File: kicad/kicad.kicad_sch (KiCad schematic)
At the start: 9 parts, among them Q1 BPW40, Q2 BP103BF, U1 PIC16F18875-E/P, U2 L293D

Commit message: finished schematic
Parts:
- added C1, C2: 0.1uF, symbol Device:C_Polarized_US
- added C3: 1000uF, symbol Device:C_Polarized_US
- added C4: C_Polarized_US, symbol Device:C_Polarized_US
- added D2: D, symbol Device:D
- added DS1: WC1602A, Display:WC1602A, symbol Display_Character:WC1602A
- added J1: ~, symbol Connector:Screw_Terminal_01x03
- added M1: Fan, symbol Motor:Fan
- added M2: Left, symbol Motor:Motor_DC
- added M3: Right, symbol Motor:Motor_DC
- added Q3: NPN, symbol Simulation_SPICE:NPN
- added R5, R6: R, symbol Device:R
- added RV1: 100k, symbol Device:R_Potentiometer
- added U3, U4: TSSP58038, OptoDevice:Vishay_MINICAST-3Pin, symbol Sensor_Proximity:TSSP58038
- added U5: L7805, symbol Regulator_Linear:L7805
- U1: footprint PDIP40_P_MCH -> (none)
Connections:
- net +5V: now also U2.16 (VCC1), U2.8 (VCC2), C1.1, C2.1, C3.1, C4.1, DS1.15 (LED(+)), DS1.2 (VDD), R5.1, R6.2, RV1.1, U3.3 (Vs), U4.3 (Vs), U5.3 (OUT)
- net GND: now also U2.12 (GND), U2.13 (GND), U2.4 (GND), U2.5 (GND), C1.2, C2.2, C3.2, C4.2, DS1.1 (VSS), DS1.16 (LED(-)), J1.2 (Pin_2), J1.3 (Pin_3), Q3.3 (E), RV1.3, U3.2 (GND), U4.2 (GND), U5.2 (GND)
- net at U2.1 (EN1,2): now also R5.2
- net RMF: now reaches U2.10 (3A)
- net RMF: now also U1.21 (RD2)
- net at U2.11 (3Y): now also M3.1 (+)
- net at U2.14 (4Y): now also M3.2 (-)
- net RMB: now reaches U2.15 (4A)
- net RMB: now also U1.22 (RD3)
- net LMF: now reaches U2.2 (1A)
- net LMF: now also U1.19 (RD0)
- net at U2.3 (1Y): now also M2.1 (+)
- net at U2.6 (2Y): now also M2.2 (-)
- net LMB: now reaches U2.7 (2A)
- net LMB: now also U1.20 (RD1)
- net at U2.9 (EN3,4): now also R6.1
- net at U1.33 (RB0): now also DS1.4 (RS)
- net at U1.34 (RB1): now also DS1.5 (R/W)
- net at U1.35 (RB2): now also DS1.6 (E)
- net at U1.37 (RB4): now also DS1.11 (D4)
- net at U1.38 (RB5): now also DS1.12 (D5)
- net at U1.39 (RB6/ICSPCLK): now also DS1.13 (D6)
- net at U1.40 (RB7/ICSPDAT): now also DS1.14 (D7)
- net at U1.5 (RA3): now also U3.1 (OUT)
- net at U1.6 (RA4): now also U4.1 (OUT)
- net fan: now reaches U1.7 (RA5)
- net fan: now also Q3.2 (B)
- new net: D2.2 (A), M1.2 (-), Q3.1 (C)
- new net: DS1.3 (VO), RV1.2
- new net +12V: D2.1 (K), M1.1 (+)
- new net +9V: J1.1 (Pin_1), U5.1 (IN)

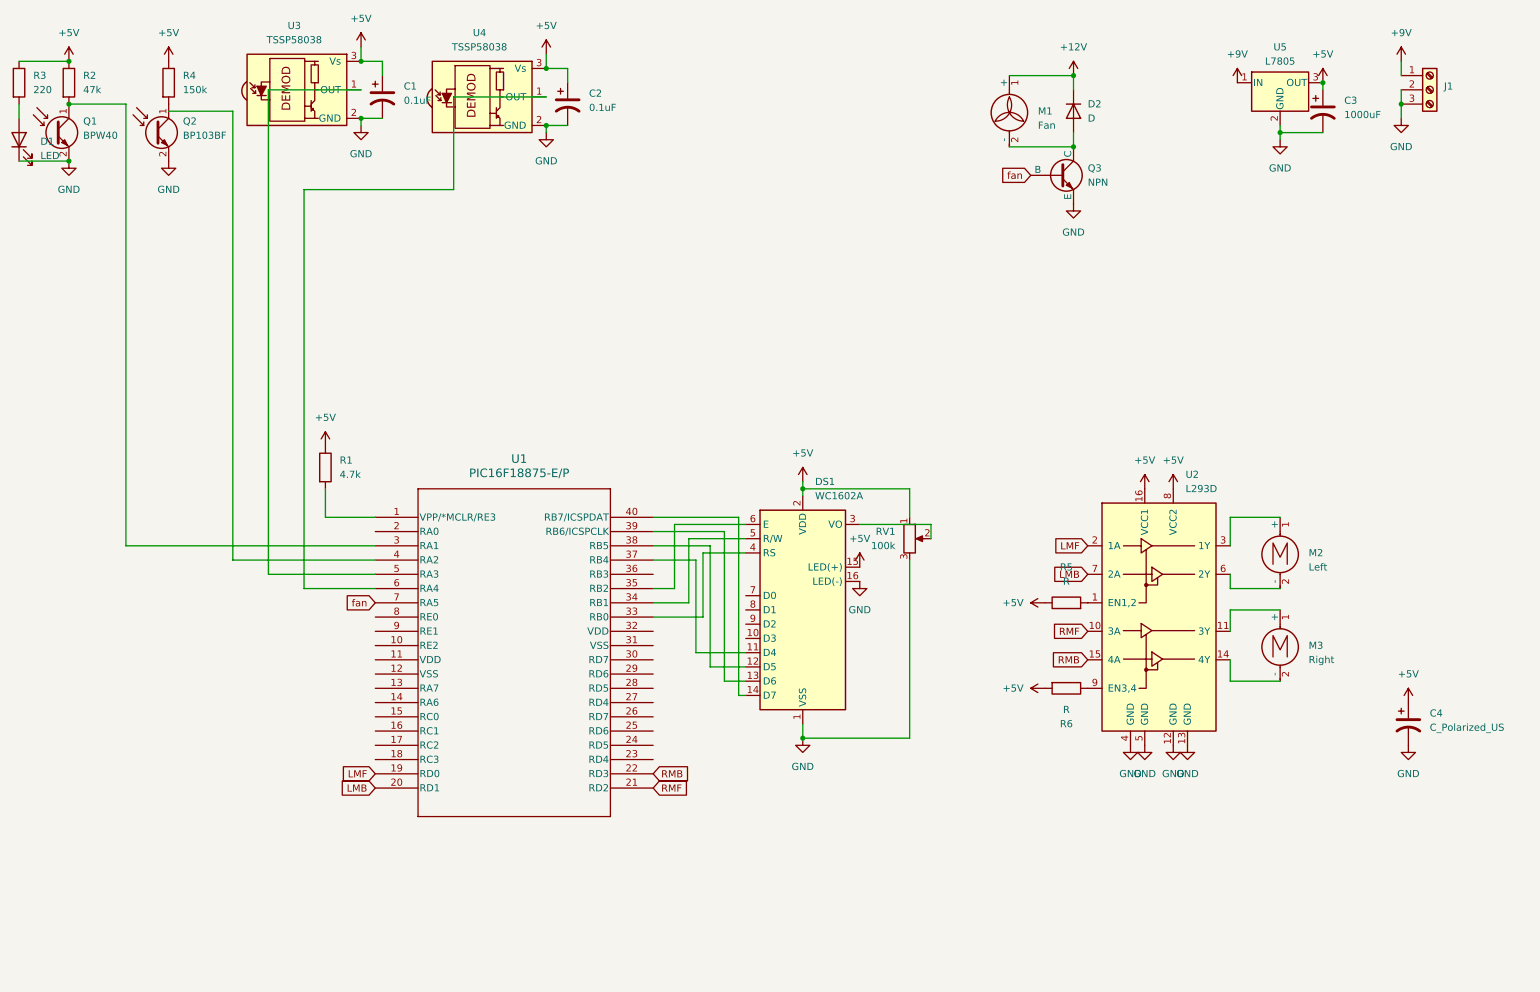
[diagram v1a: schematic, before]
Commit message: linked all footprints
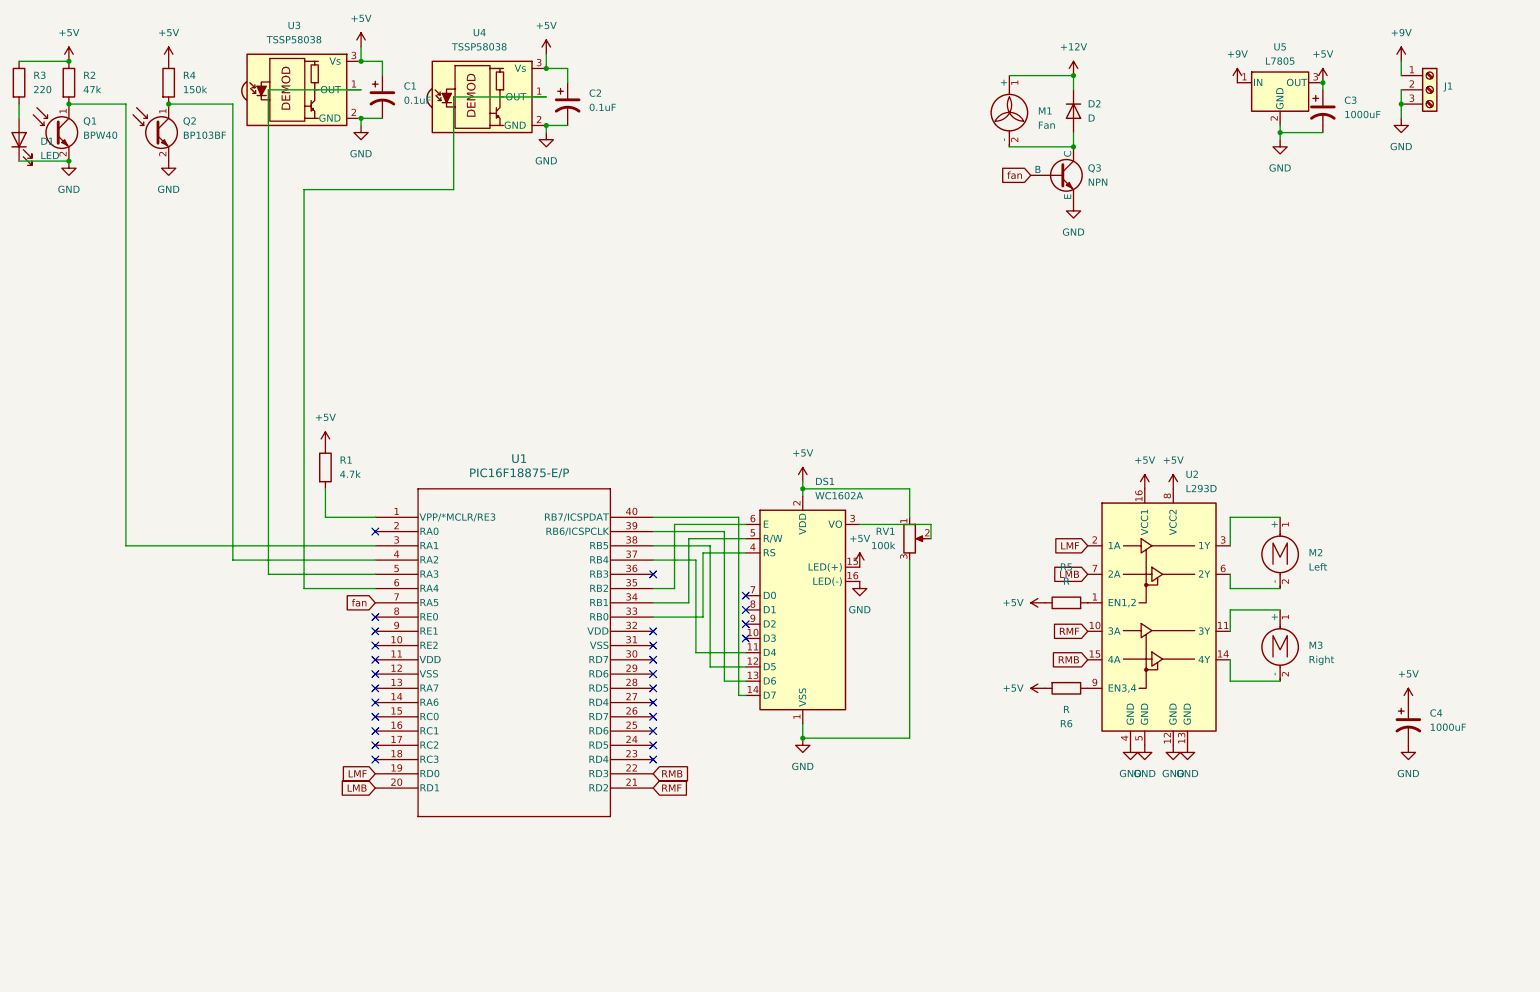
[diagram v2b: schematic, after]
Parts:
- C1, C2: footprint (none) -> EZ_TEJ_Library:C_Disc_D4.3mm_W1.9mm_P5.00mm
- C3: footprint (none) -> EZ_TEJ_Library:CP_Radial_D8.0mm_P3.80mm
- C4: value C_Polarized_US -> 1000uF; footprint (none) -> EZ_TEJ_Library:CP_Radial_D8.0mm_P3.80mm
- D1, M1, M2, M3: footprint (none) -> EZ_TEJ_Library:SolderWire-0.5sqmm_1x02_P4.6mm_D0.9mm_OD2.1mm
- D2: footprint (none) -> EZ_TEJ_Library:D_DO-41_SOD81_P7.62mm_Horizontal
- J1: footprint (none) -> EZ_TEJ_Library:TerminalBlock_Phoenix_PT-1,5-3-5.0-H_1x03_P5.00mm_Horizontal
- Q3: footprint (none) -> EZ_TEJ_Library:TO-92_Inline_Wide
- R1, R2, R3, R4, R5, R6: footprint (none) -> EZ_TEJ_Library:R_Axial_DIN0207_L6.3mm_D2.5mm_P7.62mm_Horizontal
- RV1: footprint (none) -> Potentiometer_THT:Potentiometer_Bourns_3386P_Vertical
- U1: footprint (none) -> EZ_TEJ_Library:DIP-40_W15.24mm_LongPads
- U5: footprint (none) -> EZ_TEJ_Library:TO-220-3_Vertical
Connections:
- net at Q2.1 (C), R4.2: now also U1.4 (RA2)
- no-connect marks 0 -> 27
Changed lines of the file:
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@@
 	)
 	(junction
+		(at 46.99 31.75)
+		(diameter 0)
+		(color 0 0 0 0)
+	)
+	(junction
 		(at 266.7 31.75)
 		(diameter 0)
 		(color 0 0 0 0)
 	)
+	(no_connect
+		(at 149.86 127)
+	)
+	(no_connect
+		(at 83.82 146.05)
+	)
+	(no_connect
+		(at 83.82 135.89)
+	)
+	(no_connect
+		(at 133.35 140.97)
+	)
+	(no_connect
+		(at 149.86 121.92)
+	)
+	(no_connect
+		(at 83.82 125.73)
+	)
+	(no_connect
+		(at 83.82 130.81)
+	)
+	(no_connect
+		(at 83.82 138.43)
+	)
+	(no_connect
+		(at 83.82 148.59)
+	)
+	(no_connect
+		(at 83.82 133.35)
+	)
+	(no_connect
+		(at 149.86 119.38)
+	)
+	(no_connect
+		(at 83.82 143.51)
+	)
+	(no_connect
+		(at 133.35 143.51)
+	)
+	(no_connect
+		(at 133.35 128.27)
+	)
+	(no_connect
+		(at 133.35 135.89)
+	)
+	(no_connect
+		(at 83.82 140.97)
+	)
+	(no_connect
+		(at 83.82 123.19)
+	)
+	(no_connect
+		(at 133.35 138.43)
+	)
+	(no_connect
+		(at 133.35 130.81)
+	)
+	(no_connect
+		(at 83.82 107.95)
+	)
+	(no_connect
+		(at 133.35 115.57)
+	)
+	(no_connect
+		(at 83.82 128.27)
+	)
+	(no_connect
+		(at 133.35 125.73)
+	)
+	(no_connect
+		(at 149.86 124.46)
+	)
+	(no_connect
+		(at 133.35 133.35)
+	)
+	(no_connect
+		(at 133.35 146.05)
+	)
+	(no_connect
+		(at 133.35 148.59)
+	)
 	(wire
 		(pts
@@
 	(wire
 		(pts
-			(xy 46.99 33.02) (xy 58.42 33.02)
+			(xy 46.99 31.75) (xy 58.42 31.75)
 		)
 		(stroke
@@
 	(wire
 		(pts
-			(xy 58.42 33.02) (xy 58.42 113.03)
+			(xy 58.42 31.75) (xy 58.42 113.03)
 		)
 		(stroke
@@
 			)
 		)
-		(property "Footprint" ""
+		(property "Footprint" "EZ_TEJ_Library:SolderWire-0.5sqmm_1x02_P4.6mm_D0.9mm_OD2.1mm"
 			(at 245.11 129.286 0)
 			(effects
@@
 			)
 		)
-		(property "Footprint" ""
+		(property "Footprint" "EZ_TEJ_Library:R_Axial_DIN0207_L6.3mm_D2.5mm_P7.62mm_Horizontal"
 			(at 73.152 96.52 90)
 			(effects
@@
 			)
 		)
-		(property "Value" "C_Polarized_US"
+		(property "Value" "1000uF"
 			(at 271.78 142.8749 0)
 			(effects
@@
 			)
 		)
-		(property "Footprint" ""
+		(property "Footprint" "EZ_TEJ_Library:CP_Radial_D8.0mm_P3.80mm"
 			(at 267.97 142.24 0)
 			(effects
@@
 			)
 		)
-		(property "Footprint" ""
+		(property "Footprint" "EZ_TEJ_Library:C_Disc_D4.3mm_W1.9mm_P5.00mm"
 			(at 85.09 30.48 0)
 			(effects
@@
 			)
 		)
-		(property "Footprint" ""
+		(property "Footprint" "EZ_TEJ_Library:TO-220-3_Vertical"
 			(at 245.745 31.75 0)
 			(effects
@@
 			)
 		)
-		(property "Footprint" ""
+		(property "Footprint" "EZ_TEJ_Library:R_Axial_DIN0207_L6.3mm_D2.5mm_P7.62mm_Horizontal"
 			(at 207.01 122.428 90)
 			(effects
@@
 			)
 		)
-		(property "Footprint" ""
+		(property "Footprint" "EZ_TEJ_Library:R_Axial_DIN0207_L6.3mm_D2.5mm_P7.62mm_Horizontal"
 			(at 45.212 27.94 90)
 			(effects
@@
 			)
 		)
-		(property "Footprint" ""
+		(property "Footprint" "EZ_TEJ_Library:D_DO-41_SOD81_P7.62mm_Horizontal"
 			(at 208.28 33.02 0)
 			(effects
@@
 			)
 		)
-		(property "Footprint" ""
+		(property "Footprint" "EZ_TEJ_Library:R_Axial_DIN0207_L6.3mm_D2.5mm_P7.62mm_Horizontal"
 			(at 18.542 27.94 90)
 			(effects
@@
 			)
 		)
-		(property "Footprint" ""
+		(property "Footprint" "EZ_TEJ_Library:C_Disc_D4.3mm_W1.9mm_P5.00mm"
 			(at 118.11 31.75 0)
 			(effects
@@
 			)
 		)
-		(property "Footprint" ""
+		(property "Footprint" "EZ_TEJ_Library:SolderWire-0.5sqmm_1x02_P4.6mm_D0.9mm_OD2.1mm"
 			(at 20.32 38.1 0)
 			(effects
@@
 			)
 		)
-		(property "Footprint" ""
+		(property "Footprint" "EZ_TEJ_Library:CP_Radial_D8.0mm_P3.80mm"
 			(at 252.73 33.02 0)
 			(effects
@@
 			)
 		)
-		(property "Footprint" ""
+		(property "Footprint" "EZ_TEJ_Library:SolderWire-0.5sqmm_1x02_P4.6mm_D0.9mm_OD2.1mm"
 			(at 196.85 34.036 0)
 			(effects
@@
 			)
 		)
-		(property "Footprint" ""
+		(property "Footprint" "EZ_TEJ_Library:TO-92_Inline_Wide"
 			(at 269.24 44.45 0)
 			(effects
@@
 			)
 		)
-		(property "Footprint" ""
+		(property "Footprint" "EZ_TEJ_Library:SolderWire-0.5sqmm_1x02_P4.6mm_D0.9mm_OD2.1mm"
 			(at 245.11 112.776 0)
 			(effects
@@
 			)
 		)
-		(property "Footprint" ""
+		(property "Footprint" "EZ_TEJ_Library:R_Axial_DIN0207_L6.3mm_D2.5mm_P7.62mm_Horizontal"
 			(at 207.01 134.112 90)
 			(effects
@@
 			)
 		)
-		(property "Footprint" ""
+		(property "Footprint" "EZ_TEJ_Library:R_Axial_DIN0207_L6.3mm_D2.5mm_P7.62mm_Horizontal"
 			(at 27.432 27.94 90)
 			(effects
@@
 			)
 		)
-		(property "Footprint" ""
+		(property "Footprint" "EZ_TEJ_Library:DIP-40_W15.24mm_LongPads"
 			(at 83.82 105.41 0)
 			(effects
@@
 			)
 		)
-		(property "Footprint" ""
+		(property "Footprint" "Potentiometer_THT:Potentiometer_Bourns_3386P_Vertical"
 			(at 179.07 109.22 0)
 			(effects
@@
 			)
 		)
-		(property "Footprint" ""
+		(property "Footprint" "EZ_TEJ_Library:TerminalBlock_Phoenix_PT-1,5-3-5.0-H_1x03_P5.00mm_Horizontal"
 			(at 271.78 29.21 0)
 			(effects

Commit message: components
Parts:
- added J2: headers, Connector_PinHeader_2.54mm:PinHeader_1x05_P2.54mm_Vertical, symbol Connector:Conn_01x05_Pin
- added J3: Screw_Terminal_01x05, TerminalBlock_Phoenix:TerminalBlock_Phoenix_PT-1,5-5-5.0-H_1x05_P5.00mm_Horizontal, symbol Connector:Screw_Terminal_01x08
- added J4: ~, TerminalBlock_Phoenix:TerminalBlock_Phoenix_PT-1,5-8-5.0-H_1x08_P5.00mm_Horizontal, symbol Connector:Screw_Terminal_01x08
- added SW1: SW_DIP_x01, EZ_TEJ_Library:SW_DIP_SPSTx01_Slide_9.78x4.72mm_W7.62mm_P2.54mm, symbol Switch:SW_DIP_x01
- J1: footprint EZ_TEJ_Library:TerminalBlock_Phoenix_PT-1,5-3-5.0-H_1x03_P5.00mm_Horizontal -> TerminalBlock_Phoenix:TerminalBlock_Phoenix_PT-1,5-8-5.0-H_1x08_P5.00mm_Horizontal
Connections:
- net +12V: now also J1.2 (Pin_2)
- net +5V: now also J2.2 (Pin_2), J3.6 (Pin_6), J4.6 (Pin_6)
- net +9V: now also J3.7 (Pin_7), J4.7 (Pin_7)
- net GND: now also J2.3 (Pin_3), J3.8 (Pin_8), J4.8 (Pin_8), SW1.2; no longer J1.2 (Pin_2)
- net at R1.2, U1.1 (VPP/*MCLR/RE3): now also J2.1 (Pin_1), SW1.1
- net at Q1.1 (C), R2.2: now also J4.1 (Pin_1); no longer U1.3 (RA1)
- net at DS1.13 (D6), U1.39 (RB6/ICSPCLK): now also J2.5 (Pin_5)
- net at DS1.14 (D7), U1.40 (RB7/ICSPDAT): now also J2.4 (Pin_4)
- net LMB: no longer names the net of U2.7 (2A)
- net LMB: now also J4.4 (Pin_4); no longer U1.20 (RD1)
- net LMF: no longer names the net of U2.2 (1A)
- net LMF: now also J4.5 (Pin_5); no longer U1.19 (RD0)
- net RMB: no longer names the net of U2.15 (4A)
- net RMB: now also J4.2 (Pin_2); no longer U1.22 (RD3)
- net RMF: no longer names the net of U2.10 (3A)
- net RMF: now also J4.3 (Pin_3); no longer U1.21 (RD2)
- new net: J3.4 (Pin_4), U1.19 (RD0)
- new net: J3.3 (Pin_3), U1.20 (RD1)
- new net: J3.2 (Pin_2), U1.21 (RD2)
- new net: J3.1 (Pin_1), U1.22 (RD3)
- new net: J3.5 (Pin_5), U1.3 (RA1)
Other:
- moved on the sheet: D1, Q1, R2, R3

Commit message: change pads
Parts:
- J1: footprint TerminalBlock_Phoenix:TerminalBlock_Phoenix_PT-1,5-8-5.0-H_1x08_P5.00mm_Horizontal -> TerminalBlock_Phoenix:TerminalBlock_Phoenix_PT-1,5-3-5.0-H_1x03_P5.00mm_Horizontal
- J3: footprint TerminalBlock_Phoenix:TerminalBlock_Phoenix_PT-1,5-5-5.0-H_1x05_P5.00mm_Horizontal -> TerminalBlock_Phoenix:TerminalBlock_Phoenix_PT-1,5-8-5.0-H_1x08_P5.00mm_Horizontal
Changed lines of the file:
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@@
 			)
 		)
-		(property "Footprint" "TerminalBlock_Phoenix:TerminalBlock_Phoenix_PT-1,5-8-5.0-H_1x08_P5.00mm_Horizontal"
+		(property "Footprint" "TerminalBlock_Phoenix:TerminalBlock_Phoenix_PT-1,5-3-5.0-H_1x03_P5.00mm_Horizontal"
 			(at 271.78 29.21 0)
 			(effects
@@
 			)
 		)
-		(property "Footprint" "TerminalBlock_Phoenix:TerminalBlock_Phoenix_PT-1,5-5-5.0-H_1x05_P5.00mm_Horizontal"
+		(property "Footprint" "TerminalBlock_Phoenix:TerminalBlock_Phoenix_PT-1,5-8-5.0-H_1x08_P5.00mm_Horizontal"
 			(at 99.06 180.34 0)
 			(effects

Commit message: upper board
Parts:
- added R7: 1k, EZ_TEJ_Library:R_Axial_DIN0207_L6.3mm_D2.5mm_P7.62mm_Horizontal, symbol Device:R
- Q1, Q2: footprint LED_THT:LED_D5.0mm_Clear -> EZ_TEJ_Library:SolderWire-0.5sqmm_1x02_P4.6mm_D0.9mm_OD2.1mm
- U3, U4: footprint OptoDevice:Vishay_MINICAST-3Pin -> Connector_Wire:SolderWire-0.5sqmm_1x03_P4.6mm_D0.9mm_OD2.1mm
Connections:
- net +5V: now also J3.3 (Pin_3), U1.11 (VDD), U1.32 (VDD); no longer J3.6 (Pin_6)
- net +9V: now also J3.2 (Pin_2); no longer J3.7 (Pin_7)
- net GND: now also J3.1 (Pin_1), U1.12 (VSS), U1.31 (VSS); no longer J3.8 (Pin_8)
- net fan: now also R7.2; no longer Q3.2 (B)
- net at U1.19 (RD0): now also J3.5 (Pin_5); no longer J3.4 (Pin_4)
- net at U1.20 (RD1): now also J3.6 (Pin_6); no longer J3.3 (Pin_3)
- net at U1.21 (RD2): now also J3.7 (Pin_7); no longer J3.2 (Pin_2)
- net at U1.22 (RD3): now also J3.8 (Pin_8); no longer J3.1 (Pin_1)
- net at U1.3 (RA1): now also J3.4 (Pin_4); no longer J3.5 (Pin_5)
- new net: Q3.2 (B), R7.1
- no-connect marks 27 -> 23
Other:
- moved on the sheet: J3
